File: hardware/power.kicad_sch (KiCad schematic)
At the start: 58 parts, among them Q3 AO3415A, U17 SY8088, U18 SY8088, U19 SY8089A, U20 SY8089A, U21 SY8113, U22 SY8089A

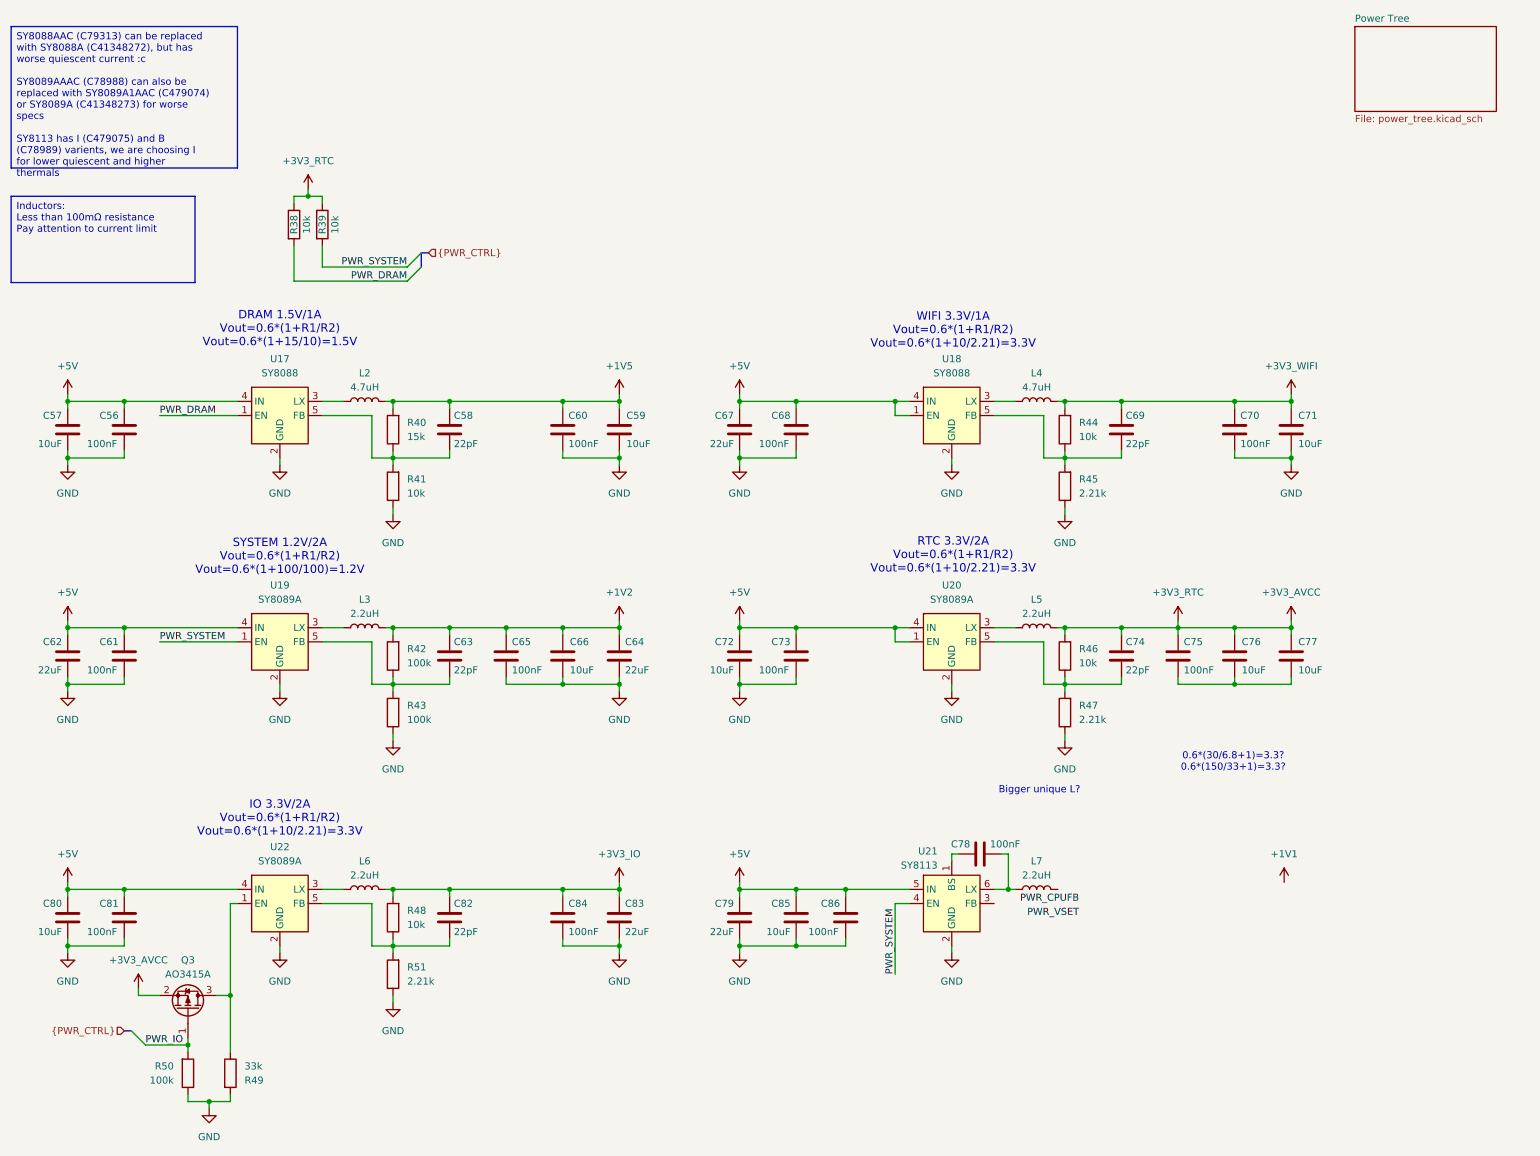
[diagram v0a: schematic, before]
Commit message: Finished DC DC converters and started decoupling the CPU
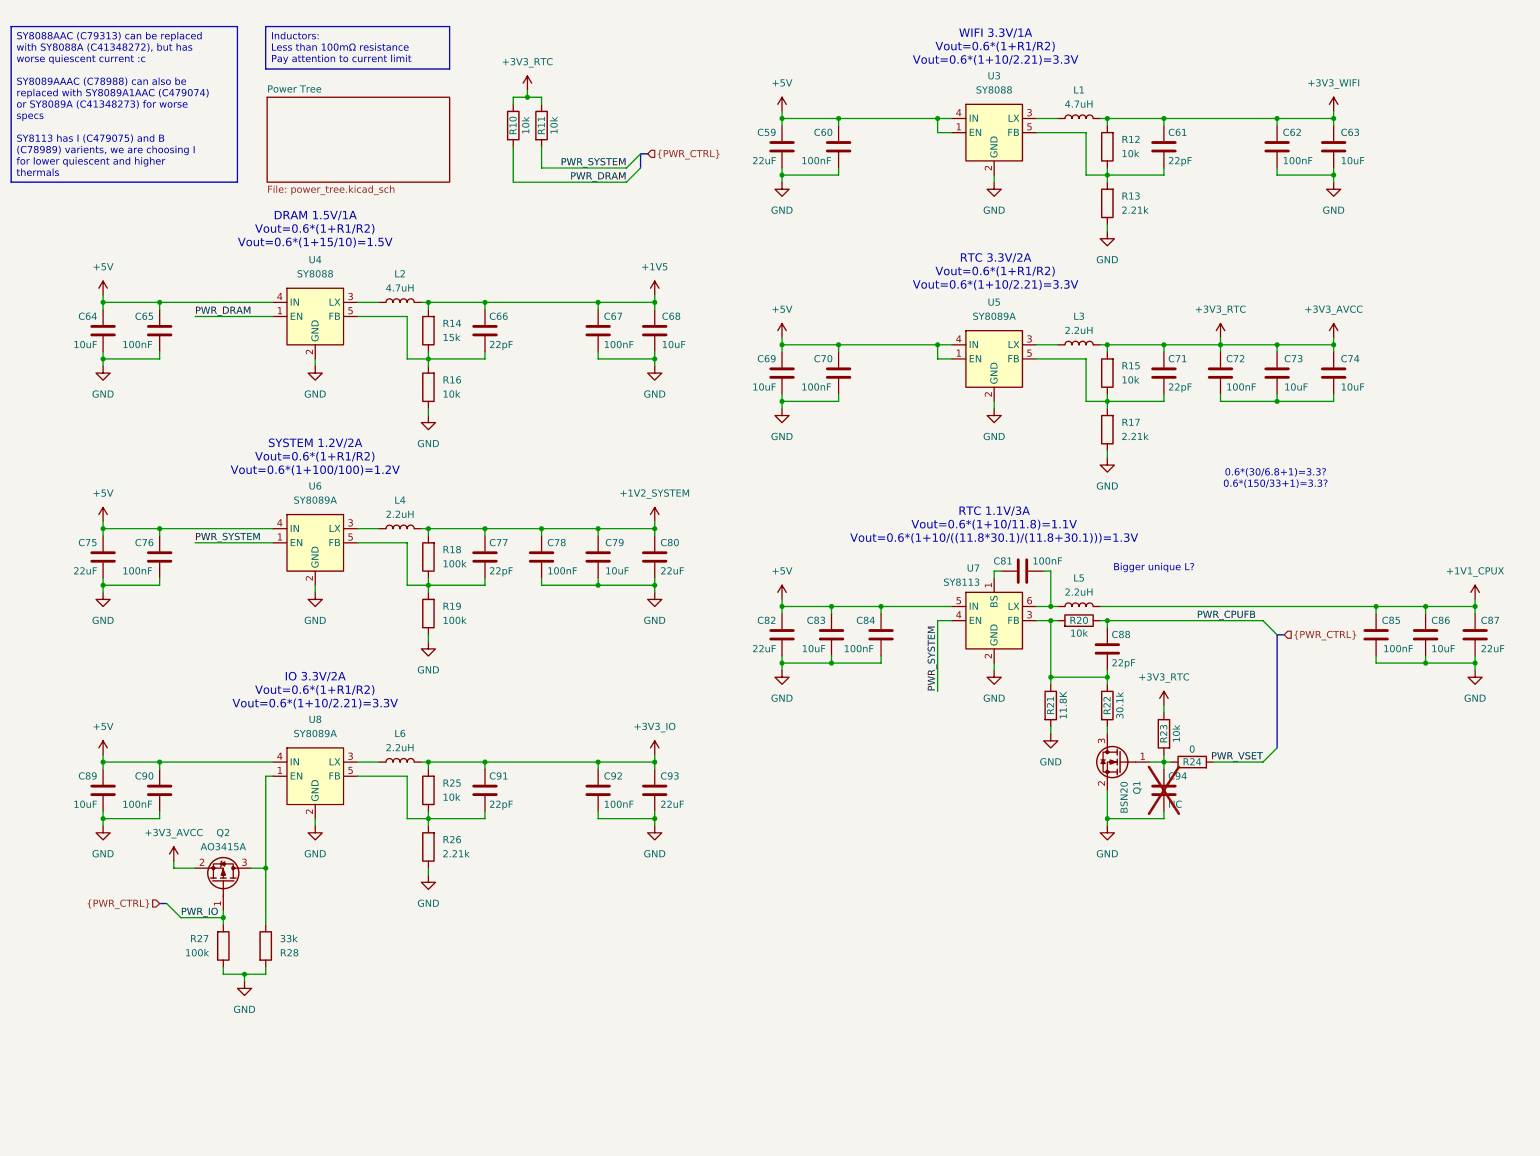
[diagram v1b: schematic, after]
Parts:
- added C85: 100nF, Capacitor_SMD:C_0402_1005Metric, symbol Device:C
- added C86: 10uF, Capacitor_SMD:C_0603_1608Metric, symbol Device:C
- added C87: 22uF, Capacitor_SMD:C_0603_1608Metric, symbol Device:C
- added C88: 22pF, Capacitor_SMD:C_0402_1005Metric, symbol Device:C
- added C94: NC, Capacitor_SMD:C_0402_1005Metric, symbol Device:C
- added Q1: BSN20, Package_TO_SOT_SMD:SOT-23, symbol Transistor_FET:BSN20
- added R20, R23: 10k, Resistor_SMD:R_0402_1005Metric, symbol Device:R
- added R21: 11.8K, Resistor_SMD:R_0402_1005Metric, symbol Device:R
- added R22: 30.1k, Resistor_SMD:R_0402_1005Metric, symbol Device:R
- added R24: 0, Resistor_SMD:R_0402_1005Metric, symbol Device:R
- renumbered C67 to C59, C68 to C60, C69 to C61, C70 to C62, C71 to C63, C57 to C64, C56 to C65, C58 to C66, C60 to C67, C59 to C68, C72 to C69, C73 to C70, C74 to C71, C75 to C72, C76 to C73, C77 to C74, C62 to C75, C61 to C76, C63 to C77, C65 to C78, C66 to C79, C64 to C80, C78 to C81, C79 to C82, C85 to C83, C86 to C84, C80 to C89, C81 to C90, C82 to C91, C84 to C92, C83 to C93, L4 to L1, L5 to L3, L3 to L4, L7 to L5, Q3 to Q2, R38 to R10, R39 to R11, R44 to R12, R45 to R13, R40 to R14, R46 to R15, R41 to R16, R47 to R17, R42 to R18, R43 to R19, R48 to R25, R51 to R26, R50 to R27, R49 to R28, U18 to U3, U17 to U4, U20 to U5, U19 to U6, U21 to U7, U22 to U8
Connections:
- net +3V3_AVCC: now also R23.1
- net GND: now also C85.1, C86.2, C87.2, C94.2, Q1.2 (S), R21.2
- net PWR_CPUFB: now also C88.1, R20.1
- net PWR_VSET: now also R24.2
- net +1V1_CPUX: now reaches L5.2
- net +1V1_CPUX: now also C85.2, C86.1, C87.1
- net at U7.3 (FB): now also C88.2, R20.2, R21.1, R22.1
- net +1V2 renamed +1V2_SYSTEM
- new net: Q1.3 (D), R22.2
- new net: C94.1, Q1.1 (G), R23.2, R24.1
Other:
- note added: "RTC 1.1V/3A Vout=0.6*(1+10/11.8)=1.1V Vout=0.6*(1+10/((11.8*30.1)/(11.8+30.1)))=1.3V"
- moved on the sheet: C59, C60, C61, C62, C63, C64, C65, C66, C67, C68, C69, C70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

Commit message: Decoupling on PCB side almost done
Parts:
- removed U5, U8: SY8089A, Package_TO_SOT_SMD:SOT-23-5, symbol cm0:SY8089A
- added U5, U8: SY8088, Package_TO_SOT_SMD:SOT-23-5, symbol cm0:SY8088
- C59, C75, C80, C82, C87, C93: LCSC Part # (none) -> C59461
- C61, C66, C71, C77, C88, C91: LCSC Part # (none) -> C1555
- L1, L2: value 4.7uH -> 2.2uH; footprint (none) -> Inductor_SMD:L_Sunlord_SWPA3015S; LCSC Part # (none) -> C19734
- L3, L6: footprint (none) -> Inductor_SMD:L_Sunlord_SWPA3015S; LCSC Part # (none) -> C19734
- L4, L5: footprint (none) -> Inductor_SMD:L_Sunlord_SWPA4030S; LCSC Part # (none) -> C135262
- R12, R15, R16, R20, R23, R25: LCSC Part # (none) -> C25744
- R13, R17, R26: value 2.21k -> 2.2k; LCSC Part # (none) -> C25879
- R14: LCSC Part # (none) -> C25756
- R18, R19, R27: LCSC Part # (none) -> C25741
- R21: LCSC Part # C25744 -> C2929934
- R22: value 30.1k -> 33k; LCSC Part # C25744 -> C25779
- R24: LCSC Part # (none) -> C17168
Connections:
- net +5V: now also U5.1 (EN), U5.4 (IN), U8.4 (IN)
- net GND: now also U5.2 (GND), U8.2 (GND)
- net at C91.2, R25.1, R26.2: now also U8.5 (FB)
- net at L6.1: now also U8.3 (LX)
- net at L3.1: now also U5.3 (LX)
- net at C71.2, R15.1, R17.2: now also U5.5 (FB)
- net at Q2.3 (D), R28.1: now also U8.1 (EN)
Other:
- note added: "CPU 1.1V/3A Vout=0.6*(1+10/11.8)=1.1V Vout=0.6*(1+10/((11.8*30.1)/(11.8+30.1)))=1.3V"
- note added: "IO 3.3V/1A Vout=0.6*(1+R1/R2) Vout=0.6*(1+10/2.21)=3.3V"
- note added: "RTC 3.3V/0.5A Vout=0.6*(1+R1/R2) Vout=0.6*(1+10/2.21)=3.3V"
- note removed: "IO 3.3V/2A Vout=0.6*(1+R1/R2) Vout=0.6*(1+10/2.21)=3.3V"
- note removed: "RTC 1.1V/3A Vout=0.6*(1+10/11.8)=1.1V Vout=0.6*(1+10/((11.8*30.1)/(11.8+30.1)))=1.3V"
- note removed: "RTC 3.3V/2A Vout=0.6*(1+R1/R2) Vout=0.6*(1+10/2.21)=3.3V"
- moved on the sheet: R10, R11

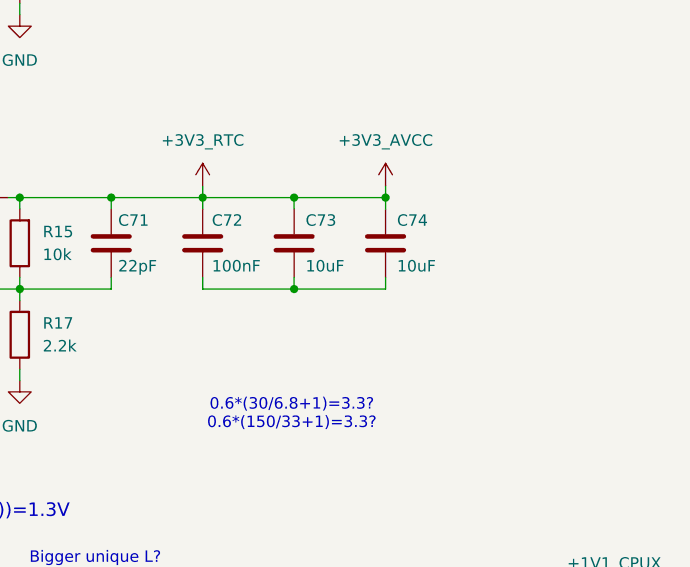
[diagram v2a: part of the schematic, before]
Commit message: Routed DCDC, EPHY and SD
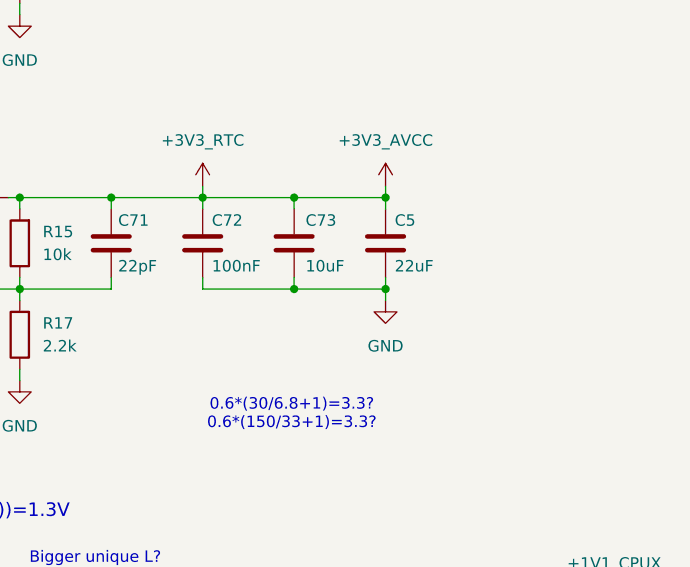
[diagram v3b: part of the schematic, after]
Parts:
- removed C74: 10uF, Capacitor_SMD:C_0603_1608Metric, symbol Device:C
- added C5: 22uF, Capacitor_SMD:C_0603_1608Metric, symbol Device:C
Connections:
- net +3V3_AVCC: now also C5.1
- net GND: now also C72.1, C73.2, C5.2
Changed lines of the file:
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@@
 	)
 	(junction
+		(at 252.73 82.55)
+		(diameter 0)
+		(color 0 0 0 0)
+	)
+	(junction
 		(at 90.17 74.93)
 		(diameter 0)
@@
 	(wire
 		(pts
+			(xy 252.73 82.55) (xy 252.73 83.82)
+		)
+		(stroke
+			(width 0)
+			(type default)
+		)
+	)
+	(wire
+		(pts
 			(xy 242.57 72.39) (xy 252.73 72.39)
 		)
@@
 	)
 	(symbol
+		(lib_id "power:GND")
+		(at 252.73 83.82 0)
+		(unit 1)
+		(exclude_from_sim no)
+		(in_bom yes)
+		(on_board yes)
+		(dnp no)
+		(fields_autoplaced yes)
+		(property "Reference" "#PWR0171"
+			(at 252.73 90.17 0)
+			(effects
+				(font
+					(size 1.27 1.27)
+				)
+				(hide yes)
+			)
+		)
+		(property "Value" "GND"
+			(at 252.73 88.9 0)
+			(effects
+				(font
+					(size 1.27 1.27)
+				)
+			)
+		)
+		(property "Footprint" ""
+			(at 252.73 83.82 0)
+			(effects
+				(font
+					(size 1.27 1.27)
+				)
+				(hide yes)
+			)
+		)
+		(property "Datasheet" ""
+			(at 252.73 83.82 0)
+			(effects
+				(font
+					(size 1.27 1.27)
+				)
+				(hide yes)
+			)
+		)
+		(property "Description" "Power symbol creates a global label with name \"GND\" , ground"
+			(at 252.73 83.82 0)
+			(effects
+				(font
+					(size 1.27 1.27)
+				)
+				(hide yes)
+			)
+		)
+		(pin "1"
+		)
+		(instances
+			(project "cm0"
+				(path "/b53f5dbb-8078-4818-9e8f-fdf90ba6d854/4796fa81-9f97-477a-89b6-db3b604885cb"
+					(reference "#PWR0171")
+					(unit 1)
+				)
+			)
+		)
+	)
+	(symbol
 		(lib_id "Device:C")
 		(at 212.09 127 0)
@@
 	)
 	(symbol
-		(lib_id "Device:C")
-		(at 252.73 77.47 0)
-		(unit 1)
-		(exclude_from_sim no)
-		(in_bom yes)
-		(on_board yes)
-		(dnp no)
-		(property "Reference" "C74"
-			(at 254 74.9298 0)
-			(effects
-				(font
-					(size 1.27 1.27)
-				)
-				(justify left)
-			)
-		)
-		(property "Value" "10uF"
-			(at 254 80.01 0)
-			(effects
-				(font
-					(size 1.27 1.27)
-				)
-				(justify left)
-			)
-		)
-		(property "Footprint" "Capacitor_SMD:C_0603_1608Metric"
-			(at 253.6952 81.28 0)
-			(effects
-				(font
-					(size 1.27 1.27)
-				)
-				(hide yes)
-			)
-		)
-		(property "Datasheet" "~"
-			(at 252.73 77.47 0)
-			(effects
-				(font
-					(size 1.27 1.27)
-				)
-				(hide yes)
-			)
-		)
-		(property "Description" "Unpolarized capacitor"
-			(at 252.73 77.47 0)
-			(effects
-				(font
-					(size 1.27 1.27)
-				)
-				(hide yes)
-			)
-		)
-		(property "LCSC Part #" "C19702"
-			(at 252.73 77.47 0)
-			(effects
-				(font
-					(size 1.27 1.27)
-				)
-				(hide yes)
-			)
-		)
-		(property "FT Position Offset" ""
-			(at 252.73 77.47 0)
-			(effects
-				(font
-					(size 1.27 1.27)
-				)
-				(hide yes)
-			)
-		)
-		(property "FT Rotation Offset" ""
-			(at 252.73 77.47 0)
-			(effects
-				(font
-					(size 1.27 1.27)
-				)
-				(hide yes)
-			)
-		)
-		(pin "1"
-		)
-		(pin "2"
-		)
-		(instances
-			(project "cm0"
-				(path "/b53f5dbb-8078-4818-9e8f-fdf90ba6d854/4796fa81-9f97-477a-89b6-db3b604885cb"
-					(reference "C74")
-					(unit 1)
-				)
-			)
-		)
-	)
-	(symbol
 		(lib_id "cm0:+3V3_AVCC")
 		(at 252.73 71.12 0)
@@
 					(unit 1)
 				)
+			)
+		)
+	)
+	(symbol
+		(lib_id "Device:C")
+		(at 252.73 77.47 0)
+		(unit 1)
+		(exclude_from_sim no)
+		(in_bom yes)
+		(on_board yes)
+		(dnp no)
+		(property "Reference" "C5"
+			(at 253.746 74.93 0)
+			(effects
+				(font
+					(size 1.27 1.27)
+				)
+				(justify left)
+			)
+		)
+		(property "Value" "22uF"
+			(at 253.746 80.0102 0)
+			(effects
+				(font
+					(size 1.27 1.27)
+				)
+				(justify left)
+			)
+		)
+		(property "Footprint" "Capacitor_SMD:C_0603_1608Metric"
+			(at 253.6952 81.28 0)
+			(effects
+				(font
+					(size 1.27 1.27)
+				)
+				(hide yes)
+			)
+		)
+		(property "Datasheet" "~"
+			(at 252.73 77.47 0)
+			(effects
+				(font
+					(size 1.27 1.27)
+				)
+				(hide yes)
+			)
+		)
+		(property "Description" "Unpolarized capacitor"
+			(at 252.73 77.47 0)
+			(effects
+				(font
+					(size 1.27 1.27)
+				)
+				(hide yes)
+			)
+		)
+		(property "LCSC Part #" "C59461"
+			(at 252.73 77.47 0)
+			(effects
+				(font
+					(size 1.27 1.27)
+				)
+				(hide yes)
+			)
+		)
+		(property "FT Position Offset" ""
+			(at 252.73 77.47 0)
+			(effects
+				(font
+					(size 1.27 1.27)
+				)
+				(hide yes)
+			)
+		)
+		(property "FT Rotation Offset" ""
+			(at 252.73 77.47 0)
+			(effects
+				(font
+					(size 1.27 1.27)
+				)
+				(hide yes)
+			)
+		)
+		(pin "1"
+		)
+		(pin "2"
+		)
+		(instances
+			(project "cm0"
+				(path "/b53f5dbb-8078-4818-9e8f-fdf90ba6d854/4796fa81-9f97-477a-89b6-db3b604885cb"
+					(reference "C5")
+					(unit 1)
+				)
